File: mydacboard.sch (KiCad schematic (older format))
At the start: 14 parts, among them J1 Conn_02x10_Odd_Even, U1 MAX9850, U2 myaudiojack

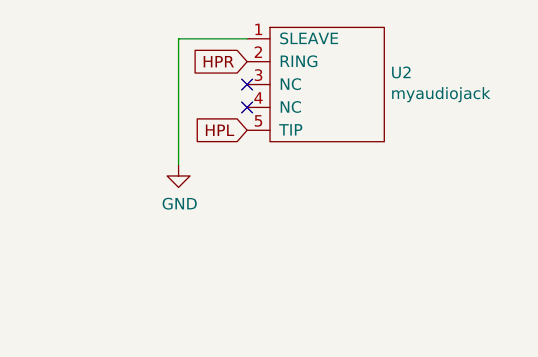
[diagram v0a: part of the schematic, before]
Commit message: Updated audiojack U->J ref
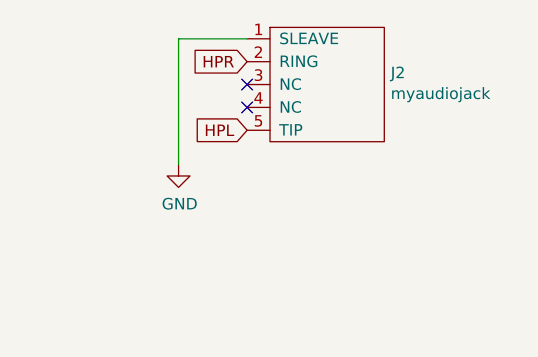
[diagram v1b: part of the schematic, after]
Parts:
- renumbered U2 to J2
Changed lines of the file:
@@
 $EndDescr
 $Comp
-L mysymbols:myaudiojack U2
+L mysymbols:myaudiojack J2
 U 1 1 61CE04F5
 P 9150 1050
-F 0 "U2" H 9428 1051 50  0000 L CNN
+F 0 "J2" H 9428 1051 50  0000 L CNN
 F 1 "myaudiojack" H 9428 960 50  0000 L CNN
 F 2 "mydacboard:myaudiojack" H 9150 600 50  0001 C CNN
